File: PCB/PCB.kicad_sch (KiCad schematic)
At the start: 7 parts, among them J1 IEC_60320_C14_Receptacle, U1 XIAO-RP2040-DIP

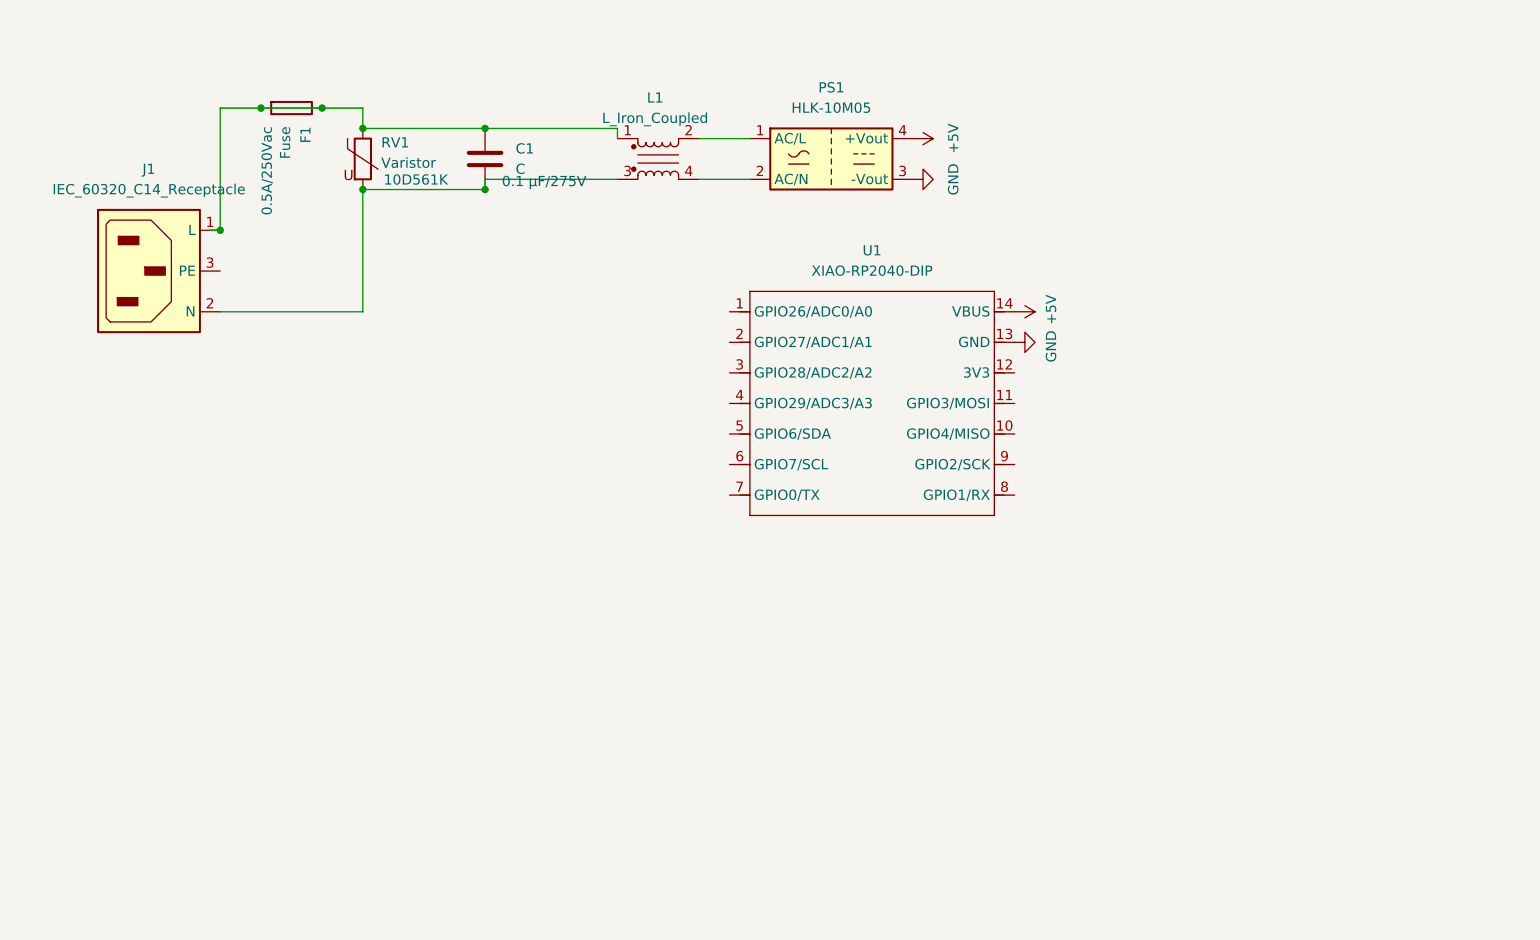
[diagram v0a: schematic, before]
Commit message: new meanwell 5v psu instead of mystery box
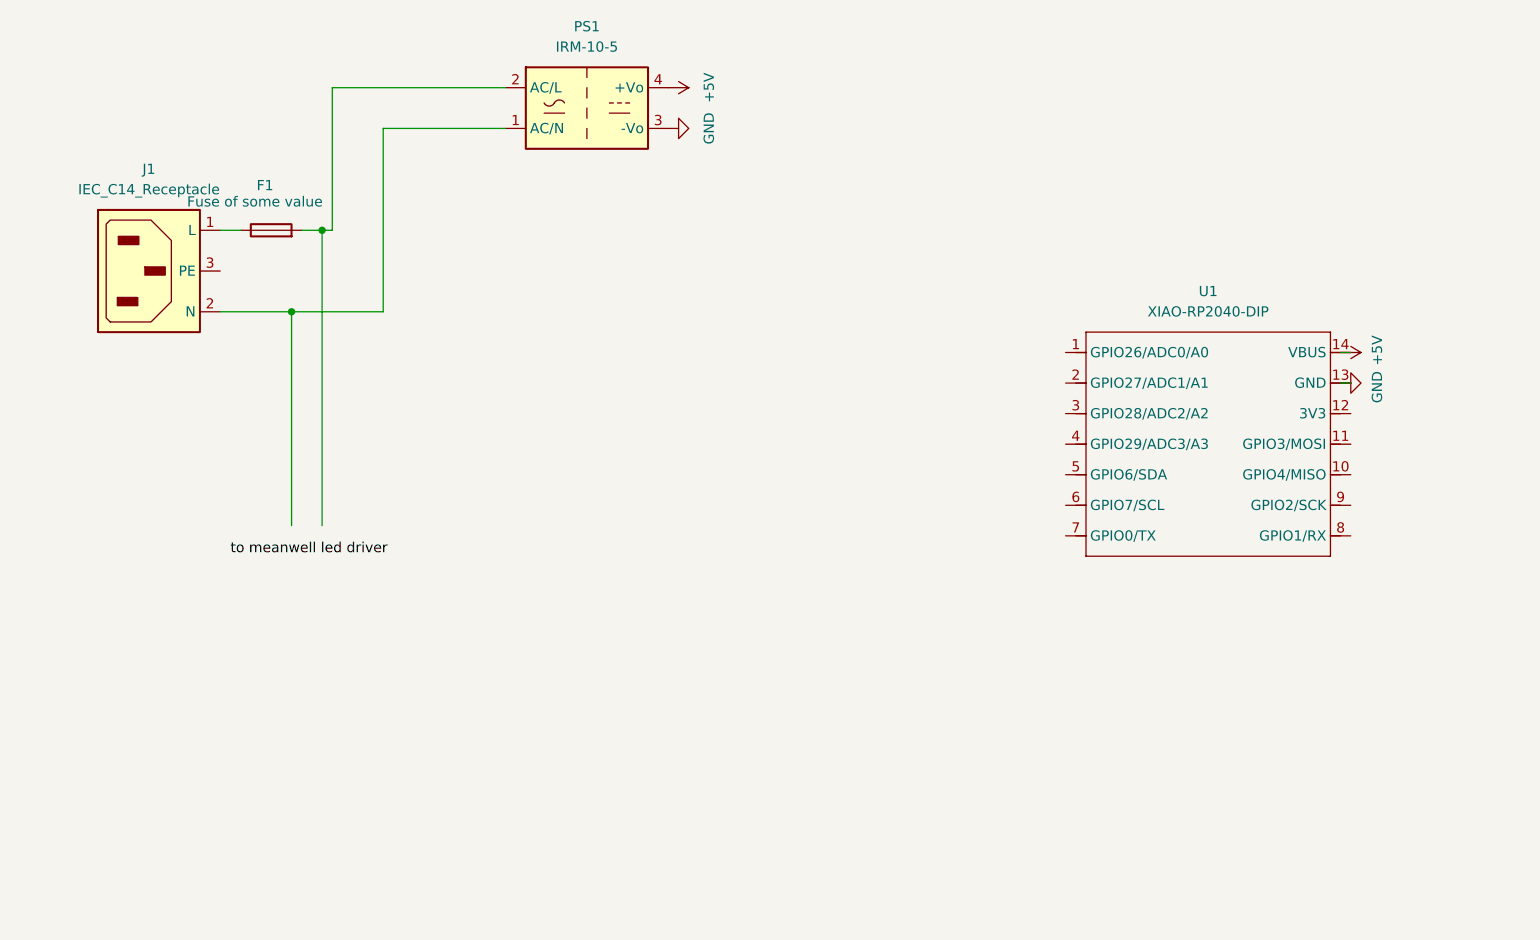
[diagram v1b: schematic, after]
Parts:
- removed C1: C, symbol Device:C
- removed L1: L_Iron_Coupled, symbol Device:L_Iron_Coupled
- removed PS1: HLK-10M05, Converter_ACDC:Converter_ACDC_Hi-Link_HLK-10Mxx, symbol Converter_ACDC:HLK-10M05
- removed RV1: Varistor, symbol Device:Varistor
- added PS1: IRM-10-5, Converter_ACDC:Converter_ACDC_MeanWell_IRM-10-xx_THT, symbol Converter_ACDC:IRM-10-5
- F1: value Fuse -> Fuse of some value; Power stuff 0.5A/250Vac -> (none)
- J1: value IEC_60320_C14_Receptacle -> IEC_C14_Receptacle
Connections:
- net +5V: now also PS1.4 (+Vo)
- net GND: now also PS1.3 (-Vo)
- net at F1.1, J1.1 (L): no longer F1.2
- net at J1.2 (N): now also PS1.1 (AC/N)
- new net: F1.2, PS1.2 (AC/L)
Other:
- moved on the sheet: U1

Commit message: made pcb better or something, oh yeah and i added the meanwell led driver as a schematic symbol
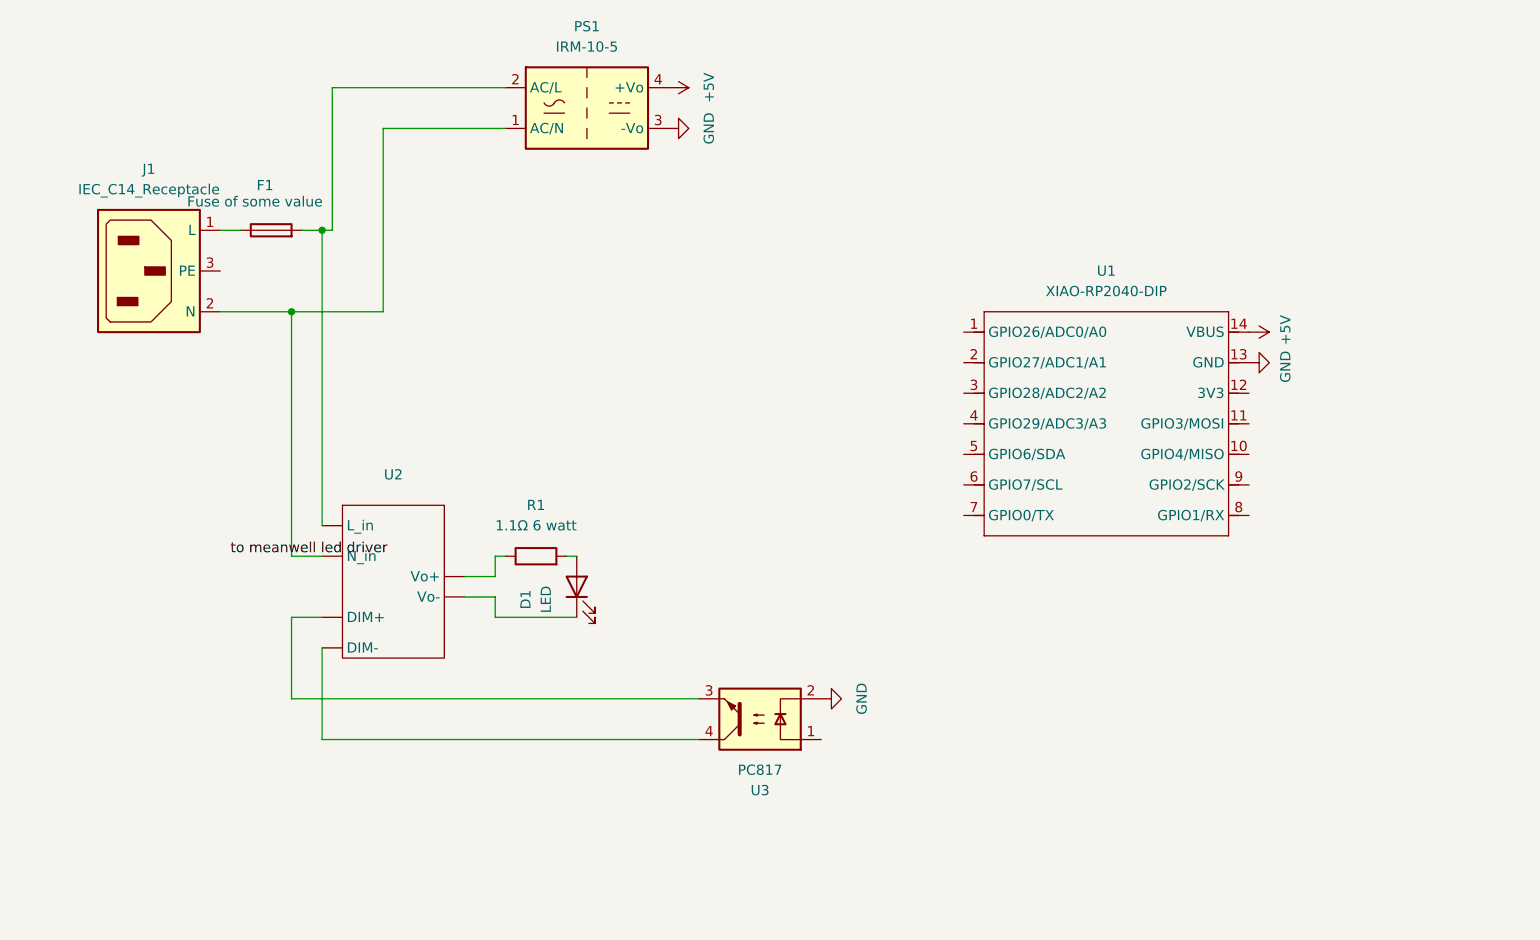
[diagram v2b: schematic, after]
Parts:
- added D1: LED, symbol Device:LED
- added R1: 1.1Ω 6 watt, symbol Device:R
- added U2: ~, symbol specialbits:Meanwell_PSU
- added U3: PC817, Package_DIP:DIP-4_W7.62mm, symbol Isolator:PC817
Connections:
- net GND: now also U3.2
- net at J1.2 (N), PS1.1 (AC/N): now also U2. (Vo-)
- net at F1.2, PS1.2 (AC/L): now also U2. (Vo-)
- new net: D1.1 (K), U2. (Vo-)
- new net: U2. (Vo-), U3.3
- new net: U2. (Vo-), U3.4
- new net: R1.1, U2. (Vo-)
- new net: D1.2 (A), R1.2
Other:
- moved on the sheet: U1

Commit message: PCB resistor
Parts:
- added R2: 42Ω 0.12W, symbol Device:R
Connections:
- net at U3.1: now also R2.2
- net at U1.4 (GPIO29/ADC3/A3): now also R2.1
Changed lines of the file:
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@@
+	(wire
+		(pts
+			(xy 123.19 125.73) (xy 123.19 119.38)
+		)
+		(stroke
+			(width 0)
+			(type default)
+		)
+	)
 	(wire
 		(pts
@@
 	(wire
 		(pts
+			(xy 123.19 111.76) (xy 123.19 86.36)
+		)
+		(stroke
+			(width 0)
+			(type default)
+		)
+	)
+	(wire
+		(pts
 			(xy 45.72 62.23) (xy 48.26 62.23)
 		)
@@
 	(wire
 		(pts
+			(xy 110.49 125.73) (xy 123.19 125.73)
+		)
+		(stroke
+			(width 0)
+			(type default)
+		)
+	)
+	(wire
+		(pts
 			(xy 55.88 49.53) (xy 71.12 49.53)
 		)
@@
 		(pts
 			(xy 44.45 72.39) (xy 55.88 72.39)
+		)
+		(stroke
+			(width 0)
+			(type default)
+		)
+	)
+	(wire
+		(pts
+			(xy 123.19 86.36) (xy 128.27 86.36)
 		)
 		(stroke
@@
 		)
 	)
+	(symbol
+		(lib_id "Device:R")
+		(at 123.19 115.57 0)
+		(unit 1)
+		(exclude_from_sim no)
+		(in_bom yes)
+		(on_board yes)
+		(dnp no)
+		(fields_autoplaced yes)
+		(property "Reference" "R2"
+			(at 125.73 114.2999 0)
+			(effects
+				(font
+					(size 1.27 1.27)
+				)
+				(justify left)
+			)
+		)
+		(property "Value" "42Ω  0.12W"
+			(at 125.73 116.8399 0)
+			(effects
+				(font
+					(size 1.27 1.27)
+				)
+				(justify left)
+			)
+		)
+		(property "Footprint" ""
+			(at 121.412 115.57 90)
+			(effects
+				(font
+					(size 1.27 1.27)
+				)
+				(hide yes)
+			)
+		)
+		(property "Datasheet" "~"
+			(at 123.19 115.57 0)
+			(effects
+				(font
+					(size 1.27 1.27)
+				)
+				(hide yes)
+			)
+		)
+		(property "Description" "Resistor"
+			(at 123.19 115.57 0)
+			(effects
+				(font
+					(size 1.27 1.27)
+				)
+				(hide yes)
+			)
+		)
+		(pin "2"
+		)
+		(pin "1"
+		)
+		(instances
+			(project ""
+				(path "/cb8a0eb9-023d-474b-952c-ea4eac5ee9fe"
+					(reference "R2")
+					(unit 1)
+				)
+			)
+		)
+	)

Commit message: pcbing!
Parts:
- added C1: 0.1µF, symbol Device:C
- added D2: LED red, symbol Device:LED
- added M1: Fan_4pin, Connector:FanPinHeader_1x04_P2.54mm_Vertical, symbol Motor:Fan_4pin
- added M2: Motor_Servo, Connector_PinHeader_1.00mm:PinHeader_1x04_P1.00mm_Vertical, symbol Motor:Motor_Servo
- added R4: 60Ω, symbol Device:R
- added RV1: Pot, symbol Device:R_Potentiometer
- added SW1: SW_SPST, symbol Switch:SW_SPST
- added SW2: SW_Push SET, symbol Switch:SW_Push
- added SW3: SW_Push Pos1, symbol Switch:SW_Push
- added SW4: SW_Push Pos2, symbol Switch:SW_Push
- added TC1: Thermocouple_Block, symbol Device:Thermocouple_Block
- added U4: MAX31855KASA, Package_SO:SOIC-8_3.9x4.9mm_P1.27mm, symbol Sensor_Temperature:MAX31855KASA
- added U5: SMU02L-12, SMU02L_12:SIP750W50P254L1160H1014Q4, symbol SMU02L-12:SMU02L-12
- R1: footprint (none) -> Connector:FanPinHeader_1x04_P2.54mm_Vertical
- U1: footprint Module:MOUDLE14P-XIAO-DIP-SMD -> Seeed Studio XIAO Series Library:XIAO-RP2040-DIP
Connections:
- net +5V: now also M2.2 (+), U5.2 (+VIN)
- net GND: now also C1.2, D2.1 (K), M2.3 (-), RV1.3, TC1.2 (-), U4.1 (GND), U4.2 (T-), U5.1 (-VIN)
- net at U1.1 (GPIO26/ADC0/A0): now also RV1.2
- net at U1.10 (GPIO4/MISO): now also U4.7 (SO)
- net at U1.11 (GPIO3/MOSI): now also R4.1
- net +3V3: now reaches U1.12 (3V3)
- net +3V3: now also C1.1, RV1.1, SW2.2, SW3.2, SW4.2, U4.4 (V_{CC})
- net at U1.2 (GPIO27/ADC1/A1): now also M2. (Sense)
- net at U1.3 (GPIO28/ADC2/A2): now also M2.1 (PWM)
- net at U1.5 (GPIO6/SDA): now also SW4.1
- net at U1.6 (GPIO7/SCL): now also SW3.1
- net at U1.7 (GPIO0/TX): now also SW2.1
- net at U1.8 (GPIO1/RX): now also U4.6 (~{CS})
- net at U1.9 (GPIO2/SCK): now also U4.5 (SCK)
- new net: PS1.2 (AC/L), SW1.2 (B), U2. (Vo-)
- new net: TC1.1 (+), U4.3 (T+)
- new net: D2.2 (A), R4.2
- new net: M1.1 (-), U5.3 (-VOUT)
- new net: M1.2 (+), U5.4 (+VOUT)
- new net: F1.2, SW1.1 (A)
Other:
- moved on the sheet: F1, J1, R2, U1, U3

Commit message: add all the changes i've made, sorry for not gitting it bit by bit
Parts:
- removed F1: Fuse of some value, symbol Device:Fuse
- removed R1: 1.1Ω 6 watt, Connector:FanPinHeader_1x04_P2.54mm_Vertical, symbol Device:R
- added C2: 10nF, Capacitor_SMD:C_1812_4532Metric_Pad1.57x3.40mm_HandSolder, symbol Device:C_Small
- added U6: Meanwell ELG-150-54B Other side, custom footprints and stuff:Meanwell ELG-150-54B Other Side, symbol specialbits:Meanwell_PSU_1
- C1: footprint (none) -> Capacitor_THT:C_Disc_D3.4mm_W2.1mm_P2.50mm
- D1: footprint (none) -> custom footprints and stuff:Big Lumileds LED
- D2: footprint (none) -> LED_THT:LED_D5.0mm
- J1: footprint (none) -> custom footprints and stuff:C14 Power input
- M2: footprint Connector_PinHeader_1.00mm:PinHeader_1x04_P1.00mm_Vertical -> Connector_PinHeader_2.54mm:PinHeader_1x04_P2.54mm_Vertical
- R2: footprint (none) -> Resistor_THT:R_Axial_DIN0207_L6.3mm_D2.5mm_P15.24mm_Horizontal
- R4: value 60Ω -> 40-60Ω; footprint (none) -> Resistor_THT:R_Axial_DIN0207_L6.3mm_D2.5mm_P15.24mm_Horizontal
- RV1: footprint (none) -> Potentiometer_THT:Potentiometer_Bourns_PTA6043_Single_Slide
- SW2, SW3, SW4: footprint (none) -> Button_Switch_Keyboard:SW_Cherry_MX_1.00u_PCB
- TC1: footprint (none) -> TerminalBlock_Philmore:TerminalBlock_Philmore_TB132_1x02_P5.00mm_Horizontal
- U2: value ~ -> Meanwell ELG-150-54B AC Side; footprint (none) -> custom footprints and stuff:Meanwell ELG-150-54B AC side
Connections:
- net +3V3: no longer SW2.2, SW3.2, SW4.2
- net GND: now also SW2.2, SW3.2, SW4.2; no longer TC1.2 (-), U4.2 (T-)
- net at U1.2 (GPIO27/ADC1/A1): now also M2.4 (Sense); no longer M2. (Sense)
- net at J1.2 (N), PS1.1 (AC/N): now also U2.2 (N_in); no longer U2. (Vo-)
- net at D1.1 (K): now also U6.2 (Vo-); no longer U2. (Vo-)
- net at U3.3: now also U6.3 (Dim+); no longer U2. (Vo-)
- net at U3.4: now also U6.4 (Dim-); no longer U2. (Vo-)
- net at TC1.1 (+), U4.3 (T+): now also C2.1
- net at J1.1 (L): now also PS1.2 (AC/L), SW1.1 (B), U2.1 (L_in)
- net at D1.2 (A): now also U6.1 (Vo+)
- new net: C2.2, TC1.2 (-), U4.2 (T-)
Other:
- note added: "Fused input receptacle"
- note added: "To make it work with the PCB part of kicad because the switch isn't on the pcb"
- moved on the sheet: SW1
